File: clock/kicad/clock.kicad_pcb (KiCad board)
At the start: 2 copper layers, 152.9 x 76.2 mm, 106 parts, among them J1 USB-SS-52100-001, Q1 PN2222A, SW1 HOUR, SW2 MIN, SW3 TIME, U1 74HC4060, U10 74HC4511, U11 74HC4511, U12 74HC4511, U13 74HC4511, U14 KCSC02-105, U15 KCSC02-105, U16 KCSC02-105, U17 KCSC02-105, U18 KCSC02-105, U19 KCSC02-105, U2 SN74HC74N, U20 74HC14, U21 74HC157, U22 NE555P, U3 74HC390, U4 74HC08, U5 74HC390, U6 74HC08, U7 74HC390, U8 74HC4511, U9 74HC4511

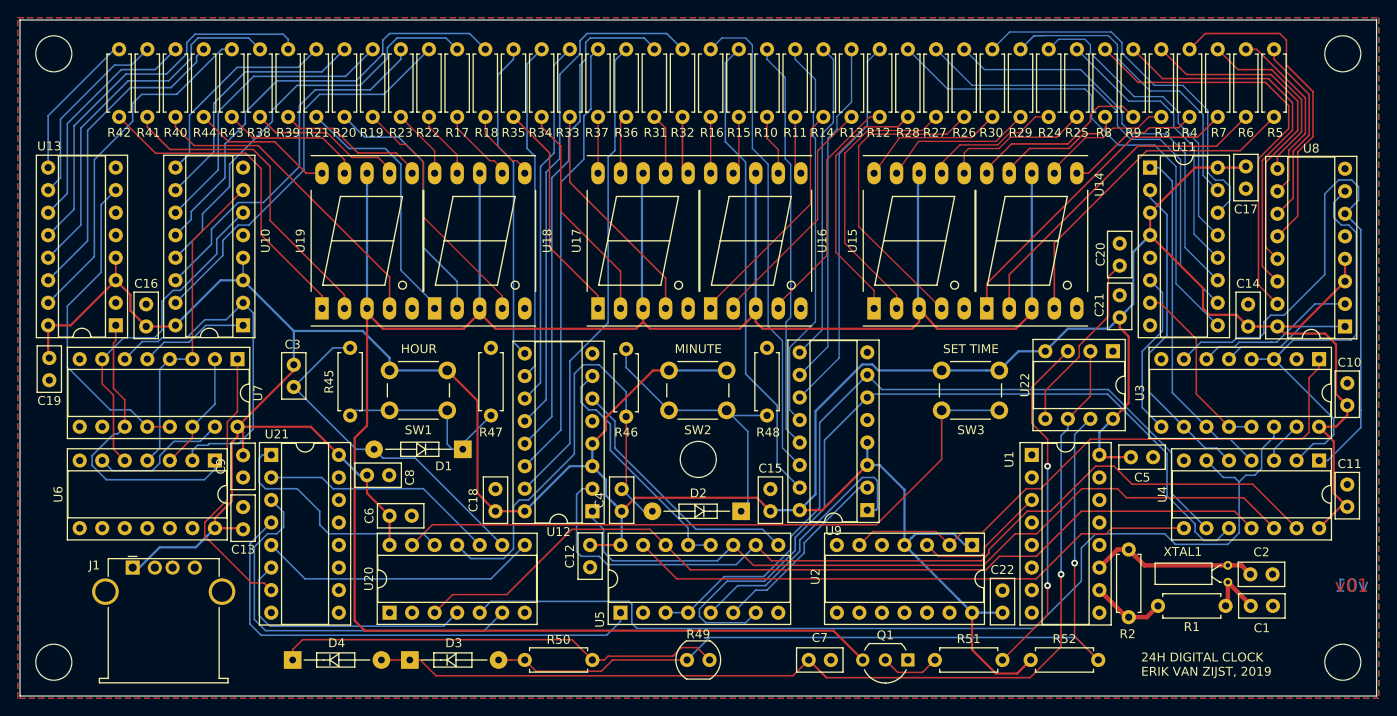
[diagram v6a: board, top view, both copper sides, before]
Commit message: Clock: Changed footprints for larger ICs.
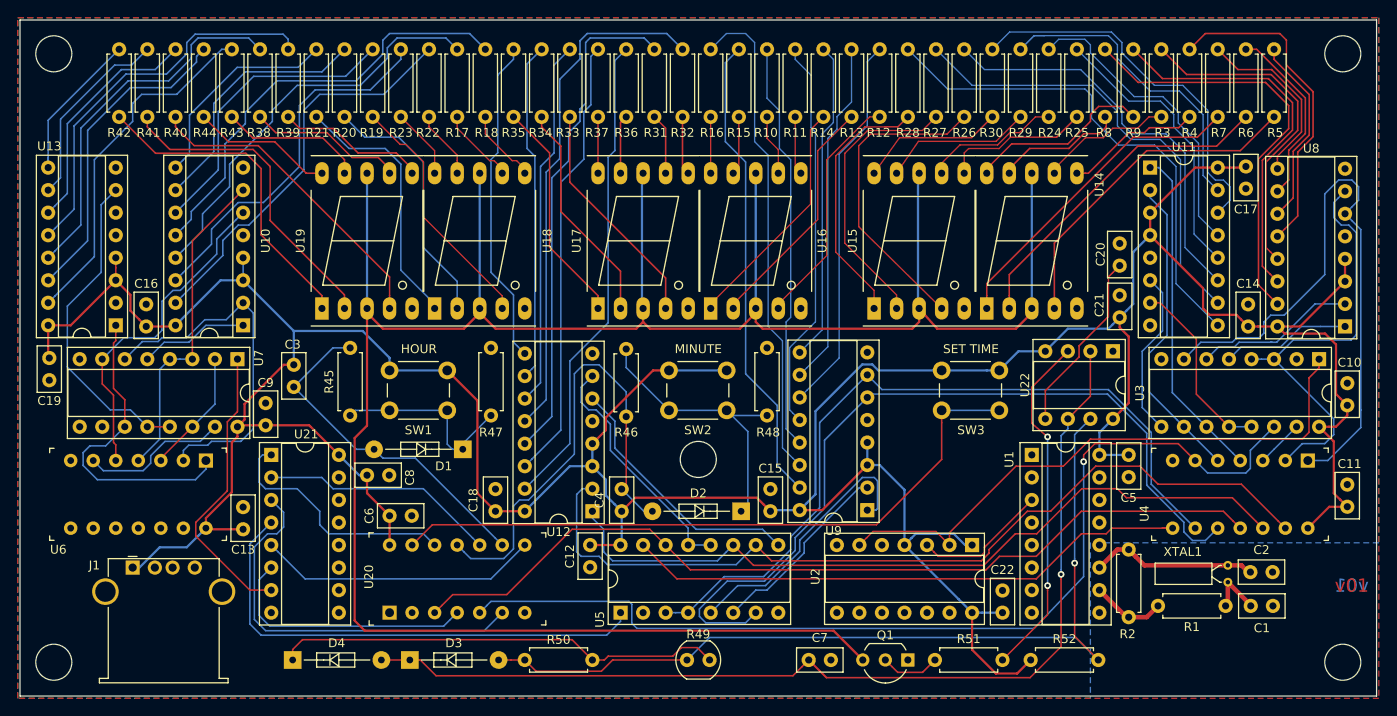
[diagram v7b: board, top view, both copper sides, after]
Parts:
- C1: value 10pF -> 20pF
- C2: value 22pF -> 20pF
- U20, U4, U6: footprint Package_DIP:DIP-14_W7.62mm_Socket -> clock:Socket_DIP-14_0.775in_Conn
- moved C9 8.76 mm to (151.9, 99.1), turned to 270 degrees
- moved U4 1.27 mm to (269.4, 105.5)
- moved U6 1.02 mm to (145.2, 105.5)
- moved C5 0.36 mm to (249.2, 104.9), turned to 270 degrees
- moved C2 0.25 mm to (262.9, 118.1)
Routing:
- net Net-(U21-Pad7): track 31.5 -> 32.9 mm
- net VCC: track 447.9 -> 446.5 mm
- net Net-(U20-Pad3): track 101.4 -> 100.1 mm
- net Net-(U12-Pad1): track 88.2 -> 86.9 mm
- net Net-(U11-Pad1): track 39.1 -> 37.8 mm
- net Net-(U3-Pad7): track 69.2 -> 70.5 mm
- net Net-(U3-Pad3): track 47.9 -> 49.2 mm
- net Net-(U12-Pad2): track 99.5 -> 98.2 mm
- net Net-(U11-Pad2): track 36.6 -> 35.3 mm
- net Net-(U13-Pad1): track 34.2 -> 35.4 mm
- net Net-(U20-Pad5): track 115.2 -> 114.0 mm, vias 0 -> 1
- net Net-(U10-Pad2): track 39.7 -> 40.7 mm
- net Net-(U6-Pad6): track 15.7 -> 16.7 mm
- net Net-(R42-Pad2): track 16.9 -> 17.8 mm
- net Net-(U2-Pad2): track 65.9 -> 66.7 mm
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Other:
- board text added: "github.com/erikvanzijst/clock erik.van.zijst@gmail.com"
- board text removed: "24H DIGITAL CLOCK ERIK VAN ZIJST, 2019"
- board text removed: "github.com/erikvanzijst/clock"

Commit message: Clock: Added voltage regulator to PCB and switched to resistor networks.
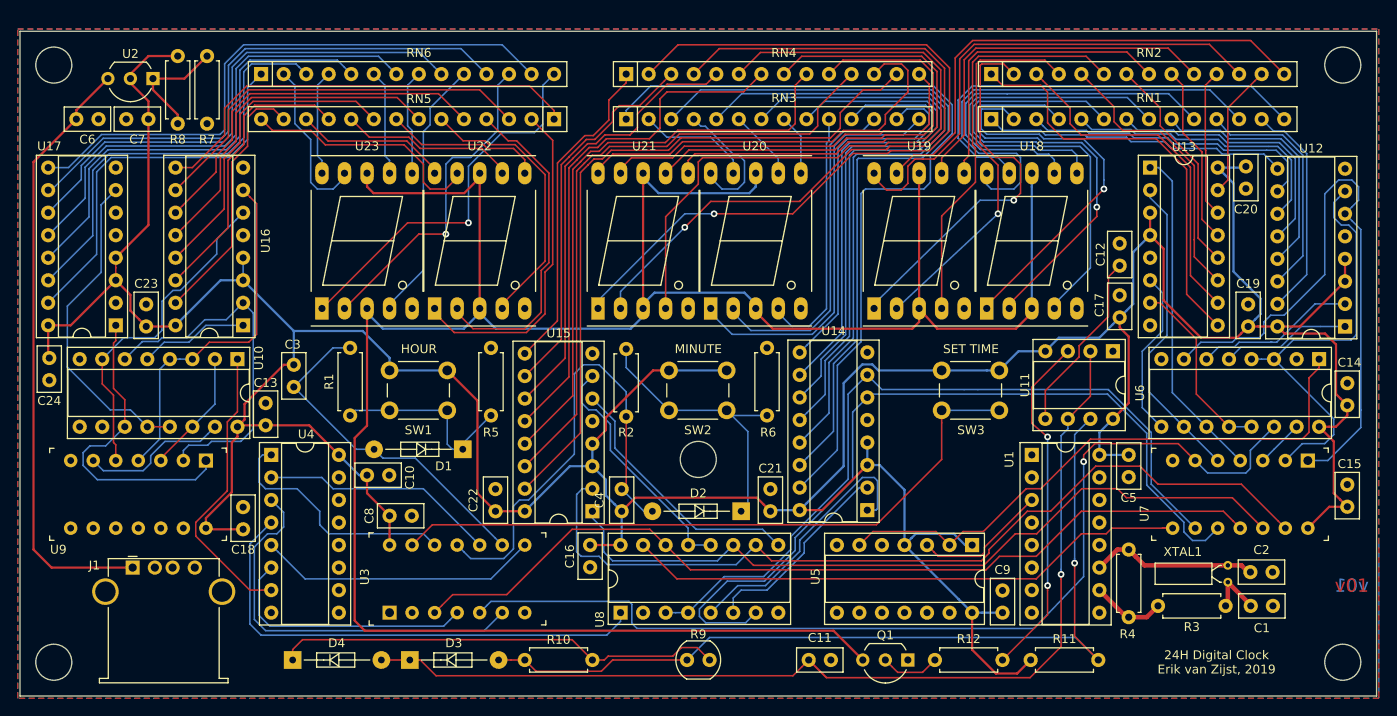
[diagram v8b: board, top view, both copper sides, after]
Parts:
- removed the R10 at (208.4, 66.8)
- removed the R11 at (211.6, 66.8)
- removed the R12 at (221.1, 66.8)
- removed R13, R14, R15, R16, R17, R18, R19, R20, R21, R22, R23, R24, R25, R26, R27, R28, R29, R30, R31, R32, R33, R34, R35, R36, R37, R38, R39, R40, R41, R42, R43, R44: 1K, Resistor_THT:R_Axial_DIN0207_L6.3mm_D2.5mm_P7.62mm_Horizontal
- removed the R3 at (252.9, 66.8)
- removed the R4 at (256.0, 66.8)
- removed the R5 at (265.6, 66.8)
- removed the R6 at (262.4, 66.8)
- removed the R9 at (249.7, 66.8)
- added C6: 10uF, Capacitor_THT:C_Disc_D5.0mm_W2.5mm_P2.50mm, F.Cu at (130.6, 67.1)
- added C7: 10uF, Capacitor_THT:C_Disc_D5.0mm_W2.5mm_P2.50mm, F.Cu at (138.7, 67.1)
- added RN1: 330, Resistor_THT:R_Array_SIP14, F.Cu at (233.7, 67.1)
- added RN2: 330, Resistor_THT:R_Array_SIP14, F.Cu at (233.7, 62.0)
- added RN3: 330, Resistor_THT:R_Array_SIP14, F.Cu at (192.5, 67.1)
- added RN4: 330, Resistor_THT:R_Array_SIP14, F.Cu at (192.5, 62.0)
- added RN5: 330, Resistor_THT:R_Array_SIP14, F.Cu at (184.4, 67.1)
- added RN6: 330, Resistor_THT:R_Array_SIP14, F.Cu at (151.4, 62.0)
- added U2: LM317L_TO92, Package_TO_SOT_THT:TO-92_Inline_Wide, F.Cu at (139.2, 62.5)
- R7: value 1K -> R
- R8: value 1K -> 120
- moved R7 114.1 mm to (145.3, 59.9), turned to 270 degrees
- moved R8 104.7 mm to (142.0, 59.9), turned to 270 degrees
- renumbered C8 to C10, C7 to C11, C20 to C12, C9 to C13, C10 to C14, C11 to C15, C12 to C16, C21 to C17, C13 to C18, C14 to C19, C17 to C20, C15 to C21, C18 to C22, C16 to C23, C19 to C24, C6 to C8, C22 to C9, R45 to R1, R50 to R10, R52 to R11, R51 to R12, R46 to R2, R1 to R3, R2 to R4, R47 to R5, R48 to R6, R49 to R9, U7 to U10, U22 to U11, U8 to U12, U11 to U13, U9 to U14, U12 to U15, U10 to U16, U13 to U17, U14 to U18, U15 to U19, U16 to U20, U17 to U21, U18 to U22, U19 to U23, U20 to U3, U21 to U4, U2 to U5, U3 to U6, U4 to U7, U5 to U8, U6 to U9
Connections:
- J1 pad 1: VCC -> /5V
- R7 pad 2: Net-(R7-Pad2) -> GND
- R8 pad 1: Net-(R8-Pad1) -> VCC
- R8 pad 2: Net-(R8-Pad2) -> Net-(R7-Pad1)
- U12 pad 15: Net-(R8-Pad2) -> Net-(RN1-Pad13)
- U12 pad 9: Net-(R7-Pad2) -> Net-(RN1-Pad1)
- U18 pad 1: Net-(R7-Pad1) -> Net-(RN1-Pad2)
- U18 pad 9: Net-(R8-Pad1) -> Net-(RN1-Pad14)
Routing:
- net /5V: track 0.00 -> 68.6 mm
- net Net-(RN4-Pad2): track 25.5 -> 91.9 mm, vias 0 -> 1
- net Net-(RN4-Pad4): track 25.3 -> 83.3 mm, vias 0 -> 1
- net Net-(RN4-Pad6): track 26.1 -> 78.1 mm
- net Net-(RN1-Pad14): track 0.00 -> 50.9 mm
- net Net-(RN4-Pad8): track 6.61 -> 56.1 mm
- net Net-(RN6-Pad13): track 17.8 -> 65.9 mm
- net Net-(R8-Pad2): track 48.0 -> 0.00 mm
- net Net-(RN4-Pad10): track 6.88 -> 51.3 mm
- net Net-(RN1-Pad2): track 0.00 -> 43.9 mm, vias 0 -> 1
- net Net-(RN3-Pad1): track 53.5 -> 93.9 mm
- net Net-(RN2-Pad12): track 16.4 -> 56.5 mm
- net Net-(RN4-Pad12): track 6.61 -> 46.6 mm
- net Net-(RN6-Pad11): track 21.6 -> 61.6 mm
- net Net-(RN2-Pad14): track 17.0 -> 56.5 mm
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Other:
- board size 152.9 x 76.2 mm -> 152.9 x 74.9 mm
- board text added: "24H Digital Clock Erik van Zijst, 2019"
